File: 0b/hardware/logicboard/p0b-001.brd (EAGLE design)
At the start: 70 x 41 mm, 33 parts, among them IC1 7404D, IC4 LTC485S, IC5 LTC485S, J0 DC5V, J7 DIN5, J9 DIN5, X7 NELTRON-7810-XPXC

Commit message: Xbar.
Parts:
- added JMP1, JMP2, JMP3, JMP4: 0R-JUMPA, jump-0r-smd:A0R-JMP
- JP1, JP2: device pinhead:1X02 -> jumper:JP1
- R7: value 220 -> 102
- moved R5 52.6 mm to (12.5, 25.0)
- moved R1 40.2 mm to (56.0, 29.0), turned to 0 degrees
- moved D1 27.0 mm to (35.0, 15.5), turned to 180 degrees
- moved R3 6.95 mm to (56.0, 24.0), turned to 0 degrees
- moved IC1 5.00 mm to (62.0, 15.5)
- moved D2 4.92 mm to (18.0, 16.0), turned to 270 degrees
- moved C8 4.50 mm to (68.0, 16.0)
- moved R2 3.16 mm to (56.0, 26.5), turned to 0 degrees
- moved R4 2.00 mm to (15.0, 25.0)
- moved JP2 0.50 mm to (11.5, 38.5), turned to 270 degrees
- turned JP1 to 90 degrees
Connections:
- new net RX+/TX+: JMP4.2, X7.6
- new net RX-/TX-: JMP3.2, X7.3
- new net TX+/RX+: JMP2.2, X7.2
- new net TX-/RX-: JMP1.2, X7.1
- net RX+: now also JMP2.3, JMP4.1, R6.1; no longer R6.2, X7.6
- net RX-: now also JMP1.3, JMP3.1, R6.2; no longer R6.1, X7.3
- net TX+: now also JMP2.1, JMP4.3; no longer X7.2
- net TX-: now also JMP1.1, JMP3.3; no longer X7.1
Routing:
- net MIDIIN: track 12.0 -> 71.2 mm, vias 0 -> 3
- net NMIDIOUT: track 16.0 -> 68.5 mm
- net TX+/RX+: track 0.00 -> 47.9 mm, vias 0 -> 1
- net RX-/TX-: track 0.00 -> 46.6 mm
- net TX+: track 40.0 -> 85.9 mm
- net RX+: track 38.6 -> 83.8 mm, vias 1 -> 4
- net TX-: track 42.4 -> 80.3 mm, vias 0 -> 2
- net TX-/RX-: track 0.00 -> 36.9 mm
- net RX+/TX+: track 0.00 -> 36.4 mm, vias 0 -> 1
- net RX-: track 41.7 -> 71.2 mm, vias 1 -> 6
- net POE: track 55.2 -> 38.3 mm
- net MIRTN: track 54.7 -> 69.7 mm, vias 3 -> 2
- net MIDIINGND: track 50.4 -> 40.0 mm, vias 0 -> 1
- net MISND: track 26.0 -> 16.8 mm
- net MORTN: track 34.5 -> 25.6 mm, vias 1 -> 0
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- removed copper zone on layer 1, net GND
- removed copper zone on layer 16, net GND
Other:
- board text added: "1: TX- 2: TX+ 3: RX- 4: GND (TYPE A)"
- board text added: "3-221"
- board text added: "BRIDGE"
- board text added: "P0b 0.0.0-X"
- board text added: "TYPE B"
- board text removed: "1: TX- 2: TX+ 3: RX- 4: GND"
- board text removed: "2-221"
- board text removed: "A"
- board text removed: "Pineapple 0b 0.0.0-X"

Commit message: Silk.
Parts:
- renumbered JMP1 to J1, JMP2 to J2, JMP3 to J3, JMP4 to J4
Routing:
- added copper zone on layer 1, net GND
- added copper zone on layer 16, net GND
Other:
- board text removed: "221"
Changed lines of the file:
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@@
 <setting verticaltext="up"/>
 </settings>
-<grid distance="0.5" unitdist="mm" unit="mm" style="lines" multiple="2" display="yes" altdistance="50" altunitdist="mil" altunit="mil"/>
+<grid distance="1" unitdist="mm" unit="mm" style="lines" multiple="2" display="yes" altdistance="50" altunitdist="mil" altunit="mil"/>
 <layers>
 <layer number="1" name="Top" color="4" fill="1" visible="yes" active="yes"/>
@@
 <text x="64" y="10" size="1" layer="25" align="center">4-M2.3</text>
 <text x="56" y="40.5" size="1" layer="25" align="center-left">IN</text>
-<text x="4" y="1.5" size="1" layer="25" align="center">221</text>
 <text x="35" y="3" size="1" layer="25" align="center">Neltron 7810-8P8C</text>
 <text x="15.5" y="32" size="1" layer="25" rot="R90" align="center">(2012)</text>
@@
 <attribute name="VALUE" x="8.96" y="35.579" size="1.27" layer="27" ratio="10"/>
 </element>
-<element name="JMP1" library="jump-0r-smd" library_urn="urn:adsk.eagle:library:251" package="A0R-JMP" package3d_urn="urn:adsk.eagle:package:15385/1" value="0R-JUMPA" x="64" y="29" smashed="yes" rot="R90">
-<attribute name="NAME" x="69.784" y="36.238" size="1.27" layer="25" rot="R90"/>
+<element name="J1" library="jump-0r-smd" library_urn="urn:adsk.eagle:library:251" package="A0R-JMP" package3d_urn="urn:adsk.eagle:package:15385/1" value="0R-JUMPA" x="64" y="29" smashed="yes" rot="R90">
+<attribute name="NAME" x="69" y="29" size="1" layer="25" rot="R90" align="center"/>
 <attribute name="POPULARITY" value="3" x="64" y="29" size="1.778" layer="27" rot="R90" display="off"/>
 <attribute name="VALUE" x="67.986" y="28.238" size="1.27" layer="27" rot="R90"/>
 </element>
-<element name="JMP2" library="jump-0r-smd" library_urn="urn:adsk.eagle:library:251" package="A0R-JMP" package3d_urn="urn:adsk.eagle:package:15385/1" value="0R-JUMPA" x="64" y="26.5" smashed="yes" rot="R90">
-<attribute name="NAME" x="66.284" y="35.238" size="1.27" layer="25" rot="R90"/>
+<element name="J2" library="jump-0r-smd" library_urn="urn:adsk.eagle:library:251" package="A0R-JMP" package3d_urn="urn:adsk.eagle:package:15385/1" value="0R-JUMPA" x="64" y="26.5" smashed="yes" rot="R90">
+<attribute name="NAME" x="69" y="26.5" size="1" layer="25" rot="R90" align="center"/>
 <attribute name="POPULARITY" value="3" x="64" y="26.5" size="1.778" layer="27" rot="R90" display="off"/>
 <attribute name="VALUE" x="67.986" y="25.738" size="1.27" layer="27" rot="R90"/>
 </element>
-<element name="JMP3" library="jump-0r-smd" library_urn="urn:adsk.eagle:library:251" package="A0R-JMP" package3d_urn="urn:adsk.eagle:package:15385/1" value="0R-JUMPA" x="64" y="24" smashed="yes" rot="R90">
-<attribute name="NAME" x="66.284" y="36.238" size="1.27" layer="25" rot="R90"/>
+<element name="J3" library="jump-0r-smd" library_urn="urn:adsk.eagle:library:251" package="A0R-JMP" package3d_urn="urn:adsk.eagle:package:15385/1" value="0R-JUMPA" x="64" y="24" smashed="yes" rot="R90">
+<attribute name="NAME" x="69" y="24" size="1" layer="25" rot="R90" align="center"/>
 <attribute name="POPULARITY" value="3" x="64" y="24" size="1.778" layer="27" rot="R90" display="off"/>
 <attribute name="VALUE" x="67.986" y="23.238" size="1.27" layer="27" rot="R90"/>
 </element>
-<element name="JMP4" library="jump-0r-smd" library_urn="urn:adsk.eagle:library:251" package="A0R-JMP" package3d_urn="urn:adsk.eagle:package:15385/1" value="0R-JUMPA" x="64" y="21.5" smashed="yes" rot="R90">
-<attribute name="NAME" x="72.284" y="35.738" size="1.27" layer="25" rot="R90"/>
+<element name="J4" library="jump-0r-smd" library_urn="urn:adsk.eagle:library:251" package="A0R-JMP" package3d_urn="urn:adsk.eagle:package:15385/1" value="0R-JUMPA" x="64" y="21.5" smashed="yes" rot="R90">
+<attribute name="NAME" x="69" y="21.5" size="1" layer="25" rot="R90" align="center"/>
 <attribute name="POPULARITY" value="3" x="64" y="21.5" size="1.778" layer="27" rot="R90" display="off"/>
 <attribute name="VALUE" x="67.986" y="20.738" size="1.27" layer="27" rot="R90"/>
@@
 <via x="60.96" y="16.4592" extent="1-16" drill="0.3048"/>
 <via x="63.8556" y="13.8684" extent="1-16" drill="0.3048"/>
+<polygon width="0.2" layer="1">
+<vertex x="-2" y="-2"/>
+<vertex x="72" y="-2"/>
+<vertex x="72" y="42"/>
+<vertex x="-2" y="42"/>
+</polygon>
+<polygon width="0.2" layer="16">
+<vertex x="-4" y="-4"/>
+<vertex x="74" y="-4"/>
+<vertex x="74" y="44"/>
+<vertex x="-4" y="44"/>
+</polygon>
 </signal>
 <signal name="VCC" class="1">
@@
 <contactref element="IC5" pad="7"/>
 <contactref element="R6" pad="2"/>
-<contactref element="JMP1" pad="3"/>
-<contactref element="JMP3" pad="1"/>
+<contactref element="J1" pad="3"/>
+<contactref element="J3" pad="1"/>
 <wire x1="9.9822" y1="26.67" x2="9.9822" y2="25.9842" width="0.1524" layer="1"/>
 <wire x1="9.525" y1="27.1272" x2="9.9822" y2="26.67" width="0.1524" layer="1"/>
@@
 <contactref element="IC5" pad="6"/>
 <contactref element="R6" pad="1"/>
-<contactref element="JMP2" pad="3"/>
-<contactref element="JMP4" pad="1"/>
+<contactref element="J2" pad="3"/>
+<contactref element="J4" pad="1"/>
 <wire x1="9.3726" y1="24.0792" x2="9.9822" y2="24.0792" width="0.1524" layer="1"/>
 <wire x1="8.4582" y1="24.9936" x2="9.3726" y2="24.0792" width="0.1524" layer="1"/>
@@
 <signal name="TX-">
 <contactref element="IC4" pad="7"/>
-<contactref element="JMP1" pad="1"/>
-<contactref element="JMP3" pad="3"/>
+<contactref element="J1" pad="1"/>
+<contactref element="J3" pad="3"/>
 <wire x1="65.7606" y1="24.765" x2="65.7606" y2="24.003" width="0.1524" layer="1"/>
 <wire x1="66.5988" y1="25.6032" x2="65.7606" y2="24.765" width="0.1524" layer="1"/>
@@
 <signal name="TX+">
 <contactref element="IC4" pad="6"/>
-<contactref element="JMP2" pad="1"/>
-<contactref element="JMP4" pad="3"/>
+<contactref element="J2" pad="1"/>
+<contactref element="J4" pad="3"/>
 <wire x1="62.2554" y1="25.6794" x2="62.2554" y2="26.4414" width="0.1524" layer="1"/>
 <wire x1="61.341" y1="24.765" x2="61.3791" y2="24.8031" width="0.1524" layer="1"/>
@@
 <signal name="TX-/RX-">
 <contactref element="X7" pad="1"/>
-<contactref element="JMP1" pad="2"/>
+<contactref element="J1" pad="2"/>
 <wire x1="63.246" y1="28.2702" x2="63.9318" y2="28.956" width="0.1524" layer="1"/>
 <wire x1="63.246" y1="28.194" x2="63.246" y2="28.2702" width="0.1524" layer="1"/>
@@
 <signal name="TX+/RX+">
 <contactref element="X7" pad="2"/>
-<contactref element="JMP2" pad="2"/>
+<contactref element="J2" pad="2"/>
 <wire x1="64.008" y1="25.2222" x2="64.008" y2="26.4414" width="0.1524" layer="1"/>
 <wire x1="64.6176" y1="25.8318" x2="64.008" y2="25.2222" width="0.1524" layer="16"/>
@@
 <signal name="RX-/TX-">
 <contactref element="X7" pad="3"/>
-<contactref element="JMP3" pad="2"/>
+<contactref element="J3" pad="2"/>
 <wire x1="65.4558" y1="22.479" x2="64.008" y2="23.9268" width="0.1524" layer="1"/>
 <wire x1="66.4464" y1="22.479" x2="65.4558" y2="22.479" width="0.1524" layer="1"/>
@@
 <signal name="RX+/TX+">
 <contactref element="X7" pad="6"/>
-<contactref element="JMP4" pad="2"/>
+<contactref element="J4" pad="2"/>
 <wire x1="63.9318" y1="21.336" x2="63.9318" y2="21.4884" width="0.1524" layer="1"/>
 <wire x1="62.6364" y1="20.0406" x2="63.9318" y2="21.336" width="0.1524" layer="1"/>

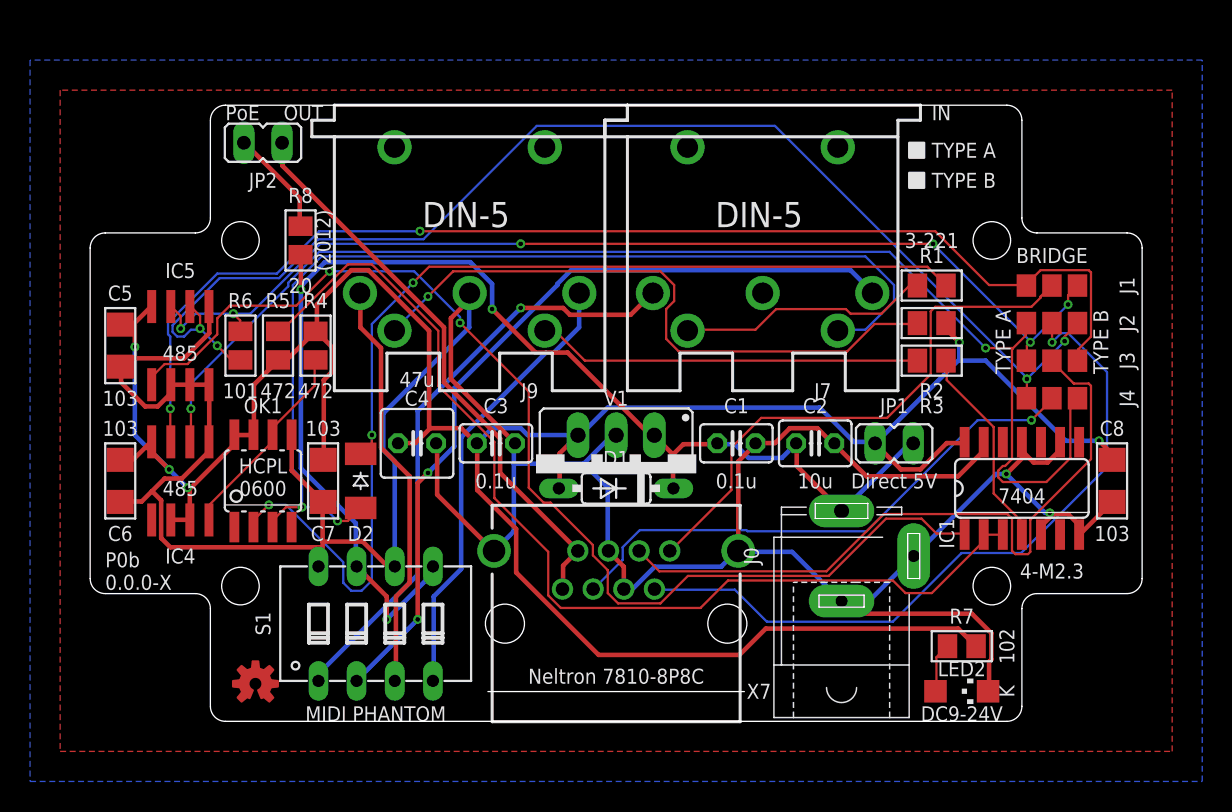
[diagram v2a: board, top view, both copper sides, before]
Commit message: Added poly sw.
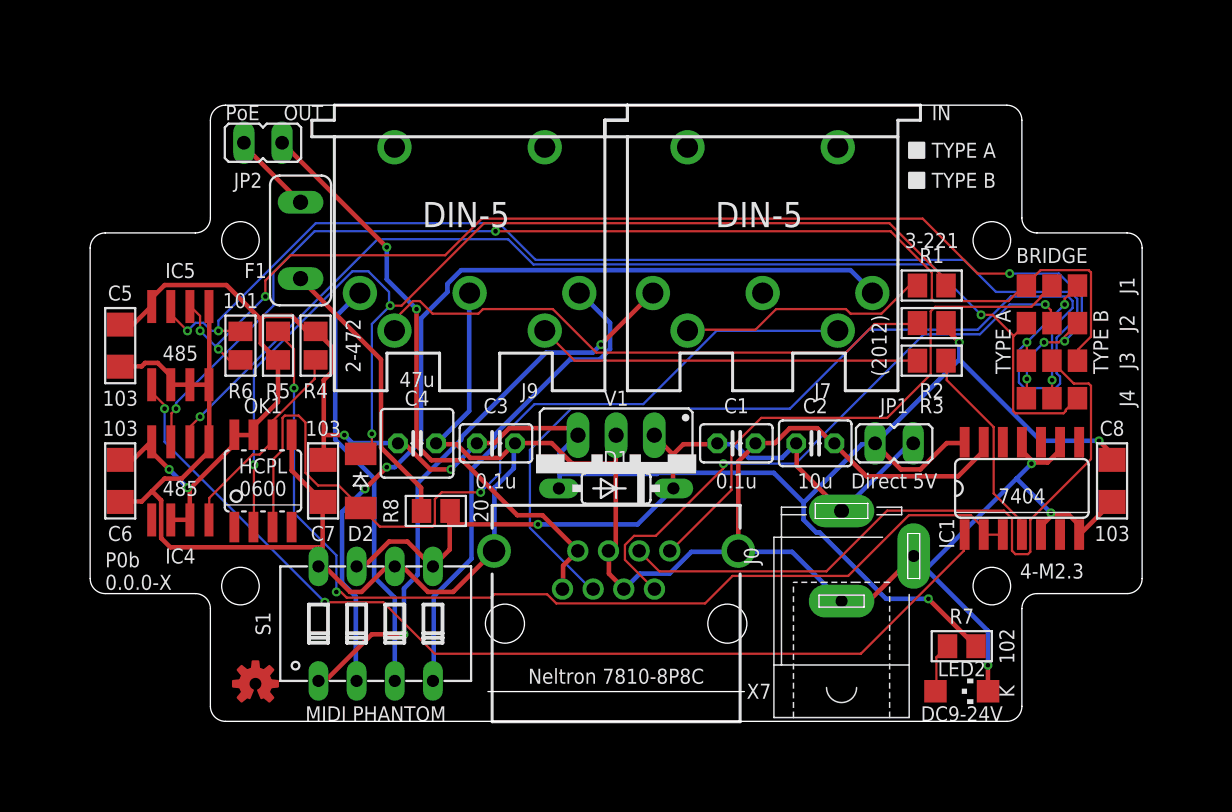
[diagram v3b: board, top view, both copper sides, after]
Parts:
- added F1: FUSETE5, fuse:TE5
- moved R8 20.1 mm to (23.0, 14.0), turned to 0 degrees
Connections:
- new net POERAW2: F1.2, R8.1
- net POERAW: now also F1.1; no longer R8.1
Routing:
- net VCC: track 180.4 -> 144.7 mm, vias 5 -> 7
- net V+: track 87.4 -> 52.2 mm, vias 3 -> 1
- net GND: track 217.4 -> 193.6 mm, vias 2 -> 3
- net RX+/TX+: track 36.4 -> 58.6 mm
- net POERAW2: track 0.00 -> 18.8 mm
- net RX-: track 71.2 -> 87.3 mm, vias 6 -> 4
- net MIRTN: track 69.7 -> 57.3 mm, vias 2 -> 1
- net TX+: track 85.9 -> 74.7 mm
- net RX: track 75.4 -> 67.1 mm
- net TX+/RX+: track 47.9 -> 40.0 mm, vias 1 -> 2
- net MIDIINV+: track 54.0 -> 59.4 mm
- net MIDIIN: track 71.2 -> 75.6 mm
- net MOSND: track 42.3 -> 38.5 mm, vias 1 -> 0
- net RX+: track 83.8 -> 80.2 mm, vias 4 -> 7
- net MIDIOUTV+: track 30.2 -> 32.7 mm
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- removed copper zone on layer 1, net GND
- removed copper zone on layer 16, net GND
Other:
- board text added: "2-472"
- board text removed: "472"

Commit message: PoE.
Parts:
- R8: device rcl:M2012 -> rcl:0204/5
- moved R8 1.12 mm to (24.0, 14.5), turned to 45 degrees
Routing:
- net MIDIIN: track 75.6 -> 56.3 mm, vias 3 -> 4
- net VCC: track 144.7 -> 161.5 mm
- net RX-: track 87.3 -> 71.4 mm
- net MIDIINGND: track 38.4 -> 51.1 mm, vias 2 -> 0
- net MIRTN: track 57.3 -> 45.7 mm, vias 1 -> 3
- net GND: track 193.6 -> 204.4 mm, vias 3 -> 4
- net MIDIINV+: track 59.4 -> 48.6 mm, vias 2 -> 3
- net RX+: track 80.2 -> 87.5 mm, vias 7 -> 4
- net TX-: track 79.9 -> 74.2 mm
- net NMIDIOUT: track 67.0 -> 72.6 mm, vias 2 -> 0
- net RX+/TX+: track 58.6 -> 53.6 mm
- net MIDIOUTV+: track 32.7 -> 34.7 mm, vias 0 -> 1
- net TX+: track 74.7 -> 72.8 mm, vias 2 -> 4
- net TX+/RX+: track 40.0 -> 38.3 mm
- net TX-/RX-: track 36.9 -> 35.3 mm
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- added copper zone on layer 1, net GND
- added copper zone on layer 16, net GND

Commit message: Fixed some errors.
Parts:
- JP1: value (none) -> Direct5V
- JP2: value (none) -> PoE
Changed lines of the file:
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@@
 <attribute name="VALUE" x="24.898025" y="11.805921875" size="1.27" layer="27" rot="R45"/>
 </element>
-<element name="JP2" library="jumper" library_urn="urn:adsk.eagle:library:252" package="JP1" package3d_urn="urn:adsk.eagle:package:15455/1" value="" x="11.5" y="38.5" smashed="yes" rot="R270">
+<element name="JP2" library="jumper" library_urn="urn:adsk.eagle:library:252" package="JP1" package3d_urn="urn:adsk.eagle:package:15455/1" value="PoE" x="11.5" y="38.5" smashed="yes" rot="R270">
 <attribute name="NAME" x="10.5" y="36" size="1" layer="25" ratio="10" align="center"/>
 <attribute name="POPULARITY" value="61" x="11.5" y="38.5" size="1.778" layer="27" rot="R270" display="off"/>
@@
 <attribute name="VALUE" x="67.986" y="20.738" size="1.27" layer="27" rot="R90"/>
 </element>
-<element name="JP1" library="jumper" library_urn="urn:adsk.eagle:library:252" package="JP1" package3d_urn="urn:adsk.eagle:package:15455/1" value="" x="53.5" y="18.5" smashed="yes" rot="R90">
+<element name="JP1" library="jumper" library_urn="urn:adsk.eagle:library:252" package="JP1" package3d_urn="urn:adsk.eagle:package:15455/1" value="Direct5V" x="53.5" y="18.5" smashed="yes" rot="R90">
 <attribute name="NAME" x="53.5" y="21" size="1" layer="25" ratio="10" align="center"/>
 <attribute name="POPULARITY" value="61" x="53.5" y="18.5" size="1.778" layer="27" rot="R90" display="off"/>
